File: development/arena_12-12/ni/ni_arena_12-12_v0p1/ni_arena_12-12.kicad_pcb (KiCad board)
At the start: 4 copper layers, 254 x 254 mm, 51 parts, among them J1 Barrel_Jack, J2 Conn_01x04, J3 Conn_01x04, P1 CONN15, P10 CONN15, P11 CONN15, P12 CONN15, P2 CONN15, P3 CONN15, P4 CONN15, P5 CONN15, P6 CONN15, P7 CONN15, P8 CONN15, P9 CONN15, Q2 MOSFET_NCHAN, SW1 SW_SPDT, U1 TXB0108PW, U18 Teensy4.1, U2 TXB0108PW, U3 TXB0108PW, U4 TXB0108PW, U5 TXB0108PW

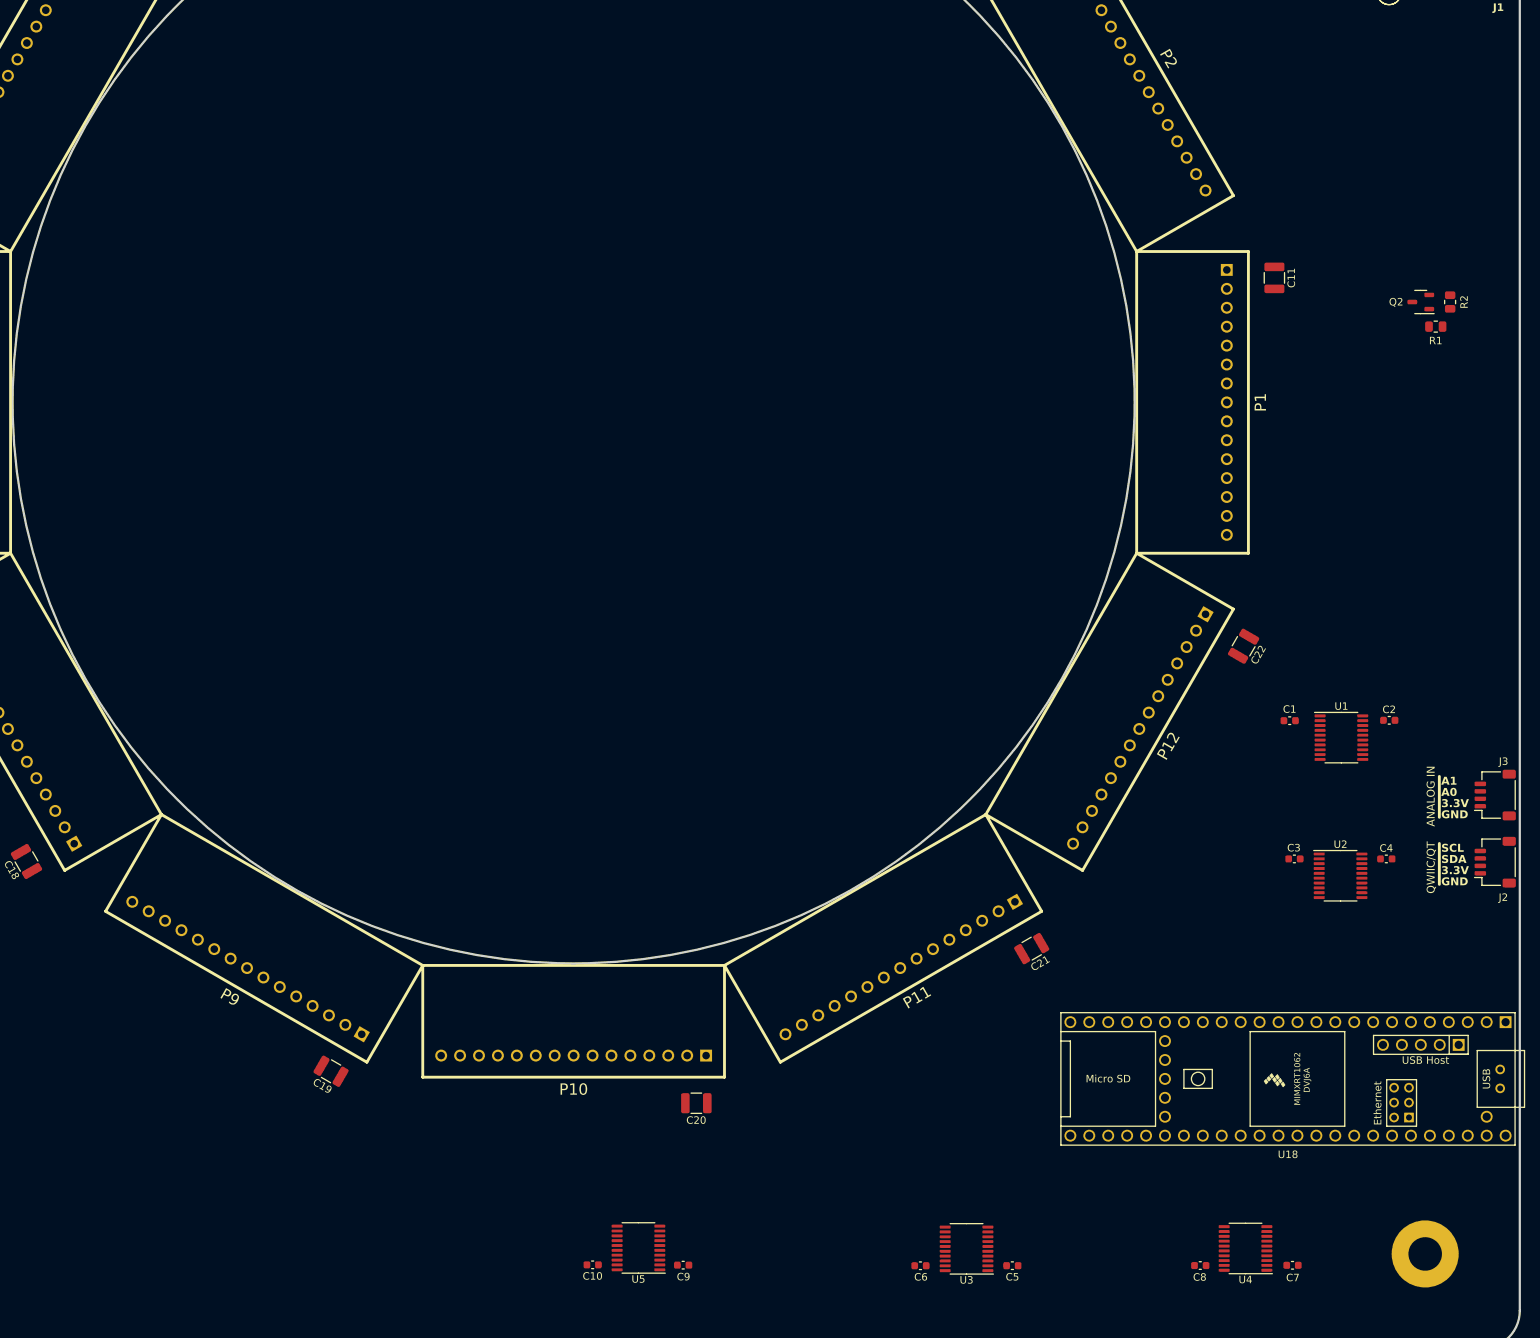
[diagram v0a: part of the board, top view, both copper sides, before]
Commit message: Finished initial schematic and layout for 12-12 NI arena (without voltage regulators).
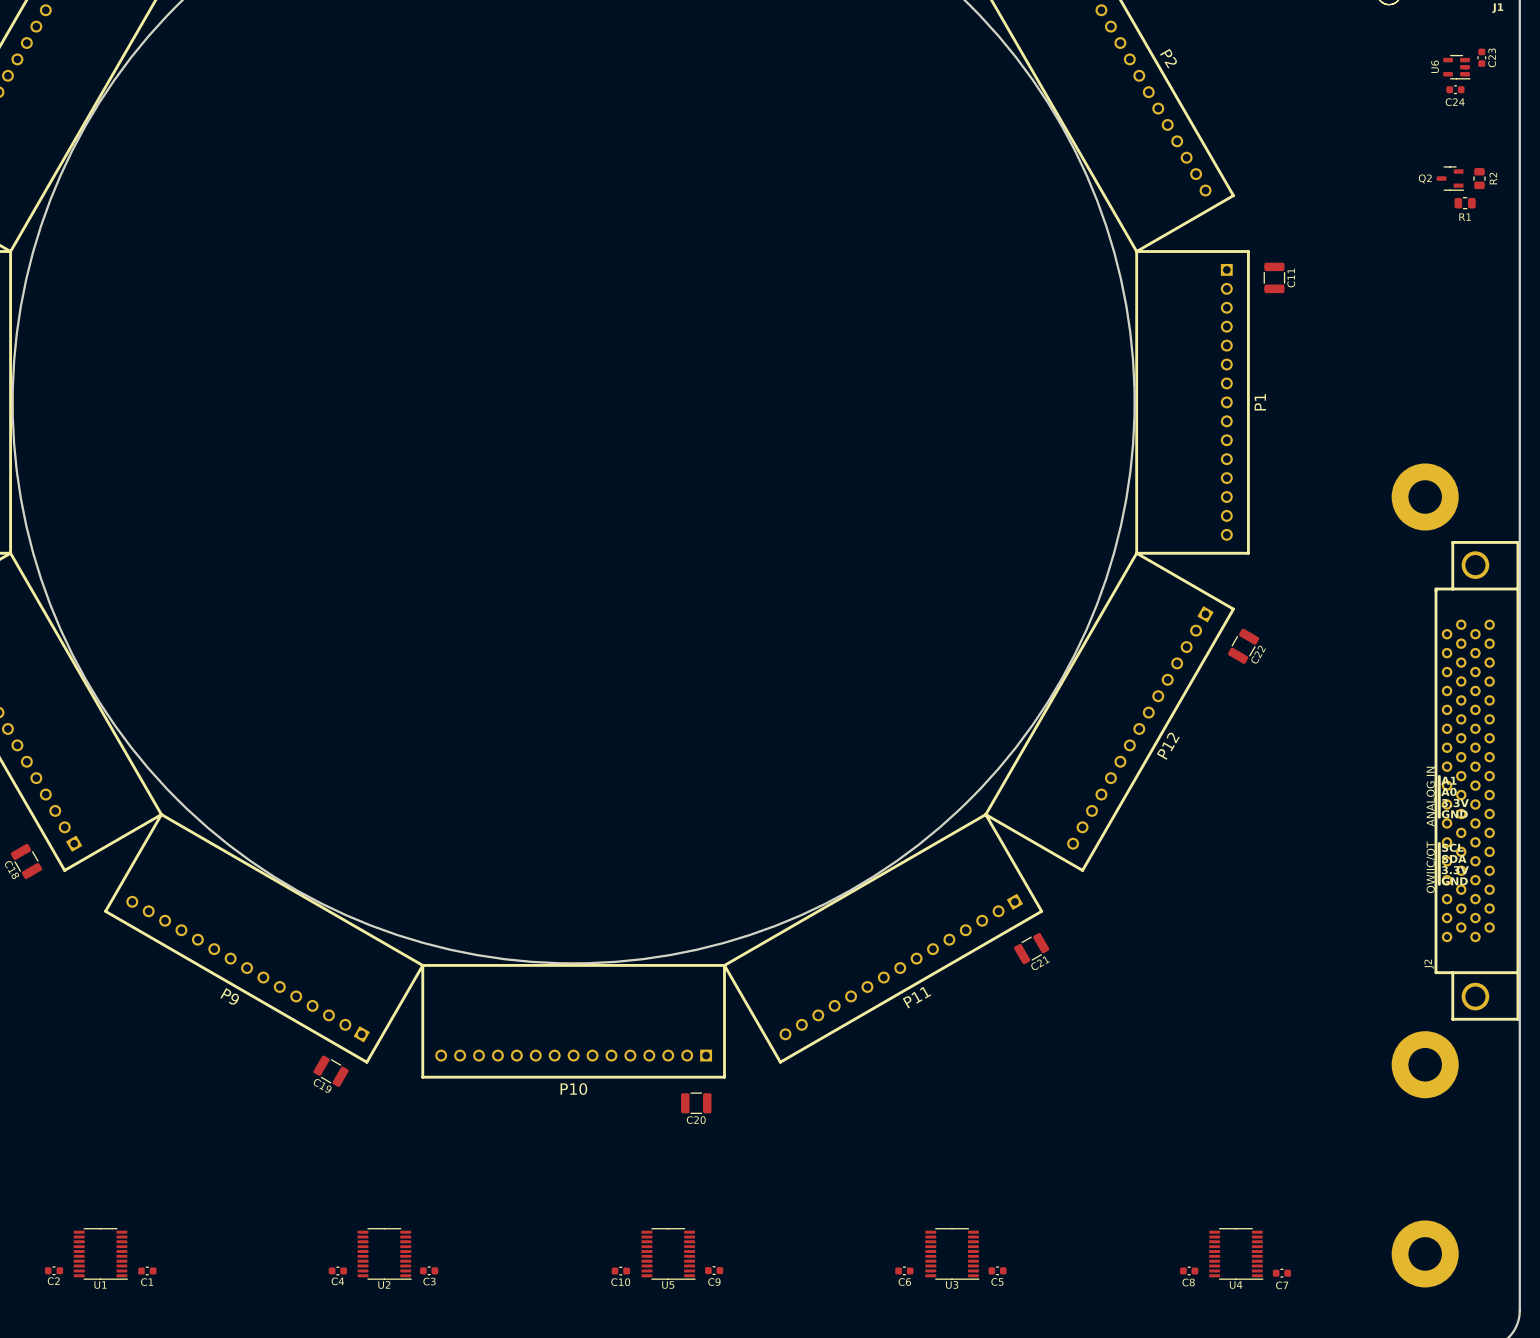
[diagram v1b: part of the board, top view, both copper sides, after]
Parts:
- removed J3: Conn_01x04, arena_custom:JST_SH_SM04B-SRSS-TB_1x04-1MP_P1.00mm_Horizontal
- removed U18: Teensy4.1, teensy:Teensy41
- added C23: 10uF, Capacitor_SMD:C_0603_1608Metric, F.Cu at (299.7, 131.5)
- added C24: 10uF, Capacitor_SMD:C_0603_1608Metric, F.Cu at (296.2, 135.8)
- added H5: MountingHole_Pad, MountingHole:MountingHole_4.5mm_Pad, F.Cu at (292.1, 190.5)
- added H6: MountingHole_Pad, MountingHole:MountingHole_4.5mm_Pad, F.Cu at (292.1, 266.7)
- added U6: AP2112K-3.3, Package_TO_SOT_SMD:SOT-23-5, F.Cu at (296.3, 132.8)
- J2: value Conn_01x04 -> NI_TE_68pos; footprint arena_custom:JST_SH_SM04B-SRSS-TB_1x04-1MP_P1.00mm_Horizontal -> arena_custom:TE_CONN_DSUB_RA_68
- moved C2 193.9 mm to (108.1, 294.4), turned to 180 degrees
- moved U1 180.4 mm to (114.3, 292.1), turned to 180 degrees
- moved C1 170.2 mm to (120.6, 294.4), turned to 0 degrees
- moved C4 151.2 mm to (146.2, 294.4), turned to 180 degrees
- moved U2 138.0 mm to (152.4, 292.1), turned to 180 degrees
- moved C3 128.6 mm to (158.4, 294.4), turned to 0 degrees
- moved Q2 17.0 mm to (295.4, 147.8)
- moved R1 17.0 mm to (297.5, 151.1)
- moved R2 17.0 mm to (299.4, 147.8)
- moved J2 11.3 mm to (304.6, 228.6)
- moved C9 4.21 mm to (196.7, 294.3)
- moved U5 4.08 mm to (190.5, 292.1)
- moved C10 3.87 mm to (184.1, 294.4)
- moved C6 2.27 mm to (222.2, 294.4)
- moved C5 2.11 mm to (234.7, 294.4)
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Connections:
- J2 pad 2: +3.3V -> GND
- J2 pad 3: /Teensy/SDA -> GND
- J2 pad 4: /Teensy/SCL -> unconnected-(J2-Pin_4-Pad4)
- P1 pad 12: unconnected-(P1-Pad12) -> /Level Shifters/PAN5V.CS_05
- P1 pad 13: unconnected-(P1-Pad13) -> /Level Shifters/PAN5V.CS_06
- P1 pad 14: unconnected-(P1-Pad14) -> /Level Shifters/PAN5V.CS_07
- P1 pad 4: /Level Shifters/PAN5V.SCK_0 -> /Level Shifters/PAN5V.SCK_00
- P1 pad 5: /Level Shifters/PAN5V.MOSI_0 -> /Level Shifters/PAN5V.MOSI_00
- P1 pad 6: /Level Shifters/PAN5V.MISO_0 -> /Level Shifters/PAN5V.MISO_00
- P10 pad 10: /Level Shifters/PAN5V.CS_18 -> /Level Shifters/PAN5V.CS_03
- P10 pad 11: /Level Shifters/PAN5V.CS_19 -> /Level Shifters/PAN5V.CS_04
- P10 pad 12: unconnected-(P10-Pad12) -> /Level Shifters/PAN5V.CS_05
- P10 pad 13: unconnected-(P10-Pad13) -> /Level Shifters/PAN5V.CS_06
- P10 pad 14: unconnected-(P10-Pad14) -> /Level Shifters/PAN5V.CS_07
- P10 pad 4: /Level Shifters/PAN5V.SCK_1 -> /Level Shifters/PAN5V.SCK_03
- P10 pad 5: /Level Shifters/PAN5V.MOSI_1 -> /Level Shifters/PAN5V.MOSI_09
- P10 pad 6: /Level Shifters/PAN5V.MISO_1 -> /Level Shifters/PAN5V.MISO_09
- P10 pad 7: /Level Shifters/PAN5V.CS_15 -> /Level Shifters/PAN5V.CS_00
- P10 pad 8: /Level Shifters/PAN5V.CS_16 -> /Level Shifters/PAN5V.CS_01
- P10 pad 9: /Level Shifters/PAN5V.CS_17 -> /Level Shifters/PAN5V.CS_02
- P11 pad 10: /Level Shifters/PAN5V.CS_23 -> /Level Shifters/PAN5V.CS_03
- P11 pad 11: /Level Shifters/PAN5V.CS_24 -> /Level Shifters/PAN5V.CS_04
- P11 pad 12: unconnected-(P11-Pad12) -> /Level Shifters/PAN5V.CS_05
- P11 pad 13: unconnected-(P11-Pad13) -> /Level Shifters/PAN5V.CS_06
- P11 pad 14: unconnected-(P11-Pad14) -> /Level Shifters/PAN5V.CS_07
- P11 pad 4: /Level Shifters/PAN5V.SCK_1 -> /Level Shifters/PAN5V.SCK_04
- P11 pad 5: /Level Shifters/PAN5V.MOSI_1 -> /Level Shifters/PAN5V.MOSI_10
- P11 pad 6: /Level Shifters/PAN5V.MISO_1 -> /Level Shifters/PAN5V.MISO_10
- P11 pad 7: /Level Shifters/PAN5V.CS_20 -> /Level Shifters/PAN5V.CS_00
- P11 pad 8: /Level Shifters/PAN5V.CS_21 -> /Level Shifters/PAN5V.CS_01
- P11 pad 9: /Level Shifters/PAN5V.CS_22 -> /Level Shifters/PAN5V.CS_02
- P12 pad 10: /Level Shifters/PAN5V.CS_28 -> /Level Shifters/PAN5V.CS_03
- P12 pad 11: /Level Shifters/PAN5V.CS_29 -> /Level Shifters/PAN5V.CS_04
- P12 pad 12: unconnected-(P12-Pad12) -> /Level Shifters/PAN5V.CS_05
- P12 pad 13: unconnected-(P12-Pad13) -> /Level Shifters/PAN5V.CS_06
- P12 pad 14: unconnected-(P12-Pad14) -> /Level Shifters/PAN5V.CS_07
- P12 pad 4: /Level Shifters/PAN5V.SCK_1 -> /Level Shifters/PAN5V.SCK_05
- P12 pad 5: /Level Shifters/PAN5V.MOSI_1 -> /Level Shifters/PAN5V.MOSI_11
- P12 pad 6: /Level Shifters/PAN5V.MISO_1 -> /Level Shifters/PAN5V.MISO_11
- P12 pad 7: /Level Shifters/PAN5V.CS_25 -> /Level Shifters/PAN5V.CS_00
- P12 pad 8: /Level Shifters/PAN5V.CS_26 -> /Level Shifters/PAN5V.CS_01
- P12 pad 9: /Level Shifters/PAN5V.CS_27 -> /Level Shifters/PAN5V.CS_02
- P2 pad 10: /Level Shifters/PAN5V.CS_08 -> /Level Shifters/PAN5V.CS_03
- P2 pad 11: /Level Shifters/PAN5V.CS_09 -> /Level Shifters/PAN5V.CS_04
- P2 pad 12: unconnected-(P2-Pad12) -> /Level Shifters/PAN5V.CS_05
- P2 pad 13: unconnected-(P2-Pad13) -> /Level Shifters/PAN5V.CS_06
- P2 pad 14: unconnected-(P2-Pad14) -> /Level Shifters/PAN5V.CS_07
- P2 pad 4: /Level Shifters/PAN5V.SCK_0 -> /Level Shifters/PAN5V.SCK_01
- P2 pad 5: /Level Shifters/PAN5V.MOSI_0 -> /Level Shifters/PAN5V.MOSI_01
- P2 pad 6: /Level Shifters/PAN5V.MISO_0 -> /Level Shifters/PAN5V.MISO_01
- P2 pad 7: /Level Shifters/PAN5V.CS_05 -> /Level Shifters/PAN5V.CS_00
- P2 pad 8: /Level Shifters/PAN5V.CS_06 -> /Level Shifters/PAN5V.CS_01
- P2 pad 9: /Level Shifters/PAN5V.CS_07 -> /Level Shifters/PAN5V.CS_02
- P3 pad 10: /Level Shifters/PAN5V.CS_13 -> /Level Shifters/PAN5V.CS_03
- P3 pad 11: /Level Shifters/PAN5V.CS_14 -> /Level Shifters/PAN5V.CS_04
- P3 pad 12: unconnected-(P3-Pad12) -> /Level Shifters/PAN5V.CS_05
- P3 pad 13: unconnected-(P3-Pad13) -> /Level Shifters/PAN5V.CS_06
- P3 pad 14: unconnected-(P3-Pad14) -> /Level Shifters/PAN5V.CS_07
- P3 pad 4: /Level Shifters/PAN5V.SCK_0 -> /Level Shifters/PAN5V.SCK_02
- P3 pad 5: /Level Shifters/PAN5V.MOSI_0 -> /Level Shifters/PAN5V.MOSI_02
- P3 pad 6: /Level Shifters/PAN5V.MISO_0 -> /Level Shifters/PAN5V.MISO_02
- P3 pad 7: /Level Shifters/PAN5V.CS_10 -> /Level Shifters/PAN5V.CS_00
- P3 pad 8: /Level Shifters/PAN5V.CS_11 -> /Level Shifters/PAN5V.CS_01
- P3 pad 9: /Level Shifters/PAN5V.CS_12 -> /Level Shifters/PAN5V.CS_02
- P4 pad 10: /Level Shifters/PAN5V.CS_18 -> /Level Shifters/PAN5V.CS_03
- P4 pad 11: /Level Shifters/PAN5V.CS_19 -> /Level Shifters/PAN5V.CS_04
- P4 pad 12: unconnected-(P4-Pad12) -> /Level Shifters/PAN5V.CS_05
- P4 pad 13: unconnected-(P4-Pad13) -> /Level Shifters/PAN5V.CS_06
- P4 pad 14: unconnected-(P4-Pad14) -> /Level Shifters/PAN5V.CS_07
- P4 pad 4: /Level Shifters/PAN5V.SCK_0 -> /Level Shifters/PAN5V.SCK_03
- P4 pad 5: /Level Shifters/PAN5V.MOSI_0 -> /Level Shifters/PAN5V.MOSI_03
- P4 pad 6: /Level Shifters/PAN5V.MISO_0 -> /Level Shifters/PAN5V.MISO_03
- P4 pad 7: /Level Shifters/PAN5V.CS_15 -> /Level Shifters/PAN5V.CS_00
- P4 pad 8: /Level Shifters/PAN5V.CS_16 -> /Level Shifters/PAN5V.CS_01
- P4 pad 9: /Level Shifters/PAN5V.CS_17 -> /Level Shifters/PAN5V.CS_02
- P5 pad 10: /Level Shifters/PAN5V.CS_23 -> /Level Shifters/PAN5V.CS_03
- P5 pad 11: /Level Shifters/PAN5V.CS_24 -> /Level Shifters/PAN5V.CS_04
- P5 pad 12: unconnected-(P5-Pad12) -> /Level Shifters/PAN5V.CS_05
- P5 pad 13: unconnected-(P5-Pad13) -> /Level Shifters/PAN5V.CS_06
- P5 pad 14: unconnected-(P5-Pad14) -> /Level Shifters/PAN5V.CS_07
- P5 pad 4: /Level Shifters/PAN5V.SCK_0 -> /Level Shifters/PAN5V.SCK_04
- P5 pad 5: /Level Shifters/PAN5V.MOSI_0 -> /Level Shifters/PAN5V.MOSI_04
- P5 pad 6: /Level Shifters/PAN5V.MISO_0 -> /Level Shifters/PAN5V.MISO_04
- P5 pad 7: /Level Shifters/PAN5V.CS_20 -> /Level Shifters/PAN5V.CS_00
- P5 pad 8: /Level Shifters/PAN5V.CS_21 -> /Level Shifters/PAN5V.CS_01
- P5 pad 9: /Level Shifters/PAN5V.CS_22 -> /Level Shifters/PAN5V.CS_02
- P6 pad 10: /Level Shifters/PAN5V.CS_28 -> /Level Shifters/PAN5V.CS_03
- P6 pad 11: /Level Shifters/PAN5V.CS_29 -> /Level Shifters/PAN5V.CS_04
- P6 pad 12: unconnected-(P6-Pad12) -> /Level Shifters/PAN5V.CS_05
- P6 pad 13: unconnected-(P6-Pad13) -> /Level Shifters/PAN5V.CS_06
- P6 pad 14: unconnected-(P6-Pad14) -> /Level Shifters/PAN5V.CS_07
- P6 pad 4: /Level Shifters/PAN5V.SCK_0 -> /Level Shifters/PAN5V.SCK_05
- P6 pad 5: /Level Shifters/PAN5V.MOSI_0 -> /Level Shifters/PAN5V.MOSI_05
- P6 pad 6: /Level Shifters/PAN5V.MISO_0 -> /Level Shifters/PAN5V.MISO_05
- P6 pad 7: /Level Shifters/PAN5V.CS_25 -> /Level Shifters/PAN5V.CS_00
- P6 pad 8: /Level Shifters/PAN5V.CS_26 -> /Level Shifters/PAN5V.CS_01
- P6 pad 9: /Level Shifters/PAN5V.CS_27 -> /Level Shifters/PAN5V.CS_02
- P7 pad 12: unconnected-(P7-Pad12) -> /Level Shifters/PAN5V.CS_05
- P7 pad 13: unconnected-(P7-Pad13) -> /Level Shifters/PAN5V.CS_06
- P7 pad 14: unconnected-(P7-Pad14) -> /Level Shifters/PAN5V.CS_07
- P7 pad 4: /Level Shifters/PAN5V.SCK_1 -> /Level Shifters/PAN5V.SCK_00
- P7 pad 5: /Level Shifters/PAN5V.MOSI_1 -> /Level Shifters/PAN5V.MOSI_06
- P7 pad 6: /Level Shifters/PAN5V.MISO_1 -> /Level Shifters/PAN5V.MISO_06
- P8 pad 10: /Level Shifters/PAN5V.CS_08 -> /Level Shifters/PAN5V.CS_03
- P8 pad 11: /Level Shifters/PAN5V.CS_09 -> /Level Shifters/PAN5V.CS_04
- P8 pad 12: unconnected-(P8-Pad12) -> /Level Shifters/PAN5V.CS_05
- P8 pad 13: unconnected-(P8-Pad13) -> /Level Shifters/PAN5V.CS_06
- P8 pad 14: unconnected-(P8-Pad14) -> /Level Shifters/PAN5V.CS_07
- P8 pad 4: /Level Shifters/PAN5V.SCK_1 -> /Level Shifters/PAN5V.SCK_01
- P8 pad 5: /Level Shifters/PAN5V.MOSI_1 -> /Level Shifters/PAN5V.MOSI_07
- P8 pad 6: /Level Shifters/PAN5V.MISO_1 -> /Level Shifters/PAN5V.MISO_07
- P8 pad 7: /Level Shifters/PAN5V.CS_05 -> /Level Shifters/PAN5V.CS_00
- P8 pad 8: /Level Shifters/PAN5V.CS_06 -> /Level Shifters/PAN5V.CS_01
- P8 pad 9: /Level Shifters/PAN5V.CS_07 -> /Level Shifters/PAN5V.CS_02
- P9 pad 10: /Level Shifters/PAN5V.CS_13 -> /Level Shifters/PAN5V.CS_03
- P9 pad 11: /Level Shifters/PAN5V.CS_14 -> /Level Shifters/PAN5V.CS_04
- P9 pad 12: unconnected-(P9-Pad12) -> /Level Shifters/PAN5V.CS_05
- P9 pad 13: unconnected-(P9-Pad13) -> /Level Shifters/PAN5V.CS_06
- P9 pad 14: unconnected-(P9-Pad14) -> /Level Shifters/PAN5V.CS_07
- P9 pad 4: /Level Shifters/PAN5V.SCK_1 -> /Level Shifters/PAN5V.SCK_02
- P9 pad 5: /Level Shifters/PAN5V.MOSI_1 -> /Level Shifters/PAN5V.MOSI_08
- P9 pad 6: /Level Shifters/PAN5V.MISO_1 -> /Level Shifters/PAN5V.MISO_08
- P9 pad 7: /Level Shifters/PAN5V.CS_10 -> /Level Shifters/PAN5V.CS_00
- P9 pad 8: /Level Shifters/PAN5V.CS_11 -> /Level Shifters/PAN5V.CS_01
- P9 pad 9: /Level Shifters/PAN5V.CS_12 -> /Level Shifters/PAN5V.CS_02
- U1 pad 1: /Level Shifters/PAN3V.RESET -> /Level Shifters/PAN3V.CS_00
- U1 pad 12: /Level Shifters/PAN5V.MISO_1 -> /Level Shifters/PAN5V.CS_07
- U1 pad 13: /Level Shifters/PAN5V.MOSI_1 -> /Level Shifters/PAN5V.CS_06
- U1 pad 14: /Level Shifters/PAN5V.SCK_1 -> /Level Shifters/PAN5V.CS_05
- U1 pad 15: unconnected-(U1-B5-Pad15) -> /Level Shifters/PAN5V.CS_04
- U1 pad 16: /Level Shifters/PAN5V.MISO_0 -> /Level Shifters/PAN5V.CS_03
- U1 pad 17: /Level Shifters/PAN5V.MOSI_0 -> /Level Shifters/PAN5V.CS_02
- U1 pad 18: /Level Shifters/PAN5V.SCK_0 -> /Level Shifters/PAN5V.CS_01
- U1 pad 20: /Level Shifters/PAN5V.RESET -> /Level Shifters/PAN5V.CS_00
- U1 pad 3: /Level Shifters/PAN3V.SCK_0 -> /Level Shifters/PAN3V.CS_01
- U1 pad 4: /Level Shifters/PAN3V.MOSI_0 -> /Level Shifters/PAN3V.CS_02
- U1 pad 5: /Level Shifters/PAN3V.MISO_0 -> /Level Shifters/PAN3V.CS_03
- U1 pad 6: unconnected-(U1-A5-Pad6) -> /Level Shifters/PAN3V.CS_04
- U1 pad 7: /Level Shifters/PAN3V.SCK_1 -> /Level Shifters/PAN3V.CS_05
- U1 pad 8: /Level Shifters/PAN3V.MOSI_1 -> /Level Shifters/PAN3V.CS_06
- U1 pad 9: /Level Shifters/PAN3V.MISO_1 -> /Level Shifters/PAN3V.CS_07
- U2 pad 1: /Level Shifters/PAN3V.CS_00 -> /Level Shifters/PAN3V.SCK_00
- U2 pad 12: /Level Shifters/PAN5V.CS_07 -> /Level Shifters/PAN5V.MISO_00
- U2 pad 13: /Level Shifters/PAN5V.CS_06 -> /Level Shifters/PAN5V.MOSI_00
- U2 pad 14: /Level Shifters/PAN5V.CS_05 -> /Level Shifters/PAN5V.SCK_05
- U2 pad 15: /Level Shifters/PAN5V.CS_04 -> /Level Shifters/PAN5V.SCK_04
- U2 pad 16: /Level Shifters/PAN5V.CS_03 -> /Level Shifters/PAN5V.SCK_03
- U2 pad 17: /Level Shifters/PAN5V.CS_02 -> /Level Shifters/PAN5V.SCK_02
- U2 pad 18: /Level Shifters/PAN5V.CS_01 -> /Level Shifters/PAN5V.SCK_01
- U2 pad 20: /Level Shifters/PAN5V.CS_00 -> /Level Shifters/PAN5V.SCK_00
- U2 pad 3: /Level Shifters/PAN3V.CS_01 -> /Level Shifters/PAN3V.SCK_01
- U2 pad 4: /Level Shifters/PAN3V.CS_02 -> /Level Shifters/PAN3V.SCK_02
- U2 pad 5: /Level Shifters/PAN3V.CS_03 -> /Level Shifters/PAN3V.SCK_03
- U2 pad 6: /Level Shifters/PAN3V.CS_04 -> /Level Shifters/PAN3V.SCK_04
- U2 pad 7: /Level Shifters/PAN3V.CS_05 -> /Level Shifters/PAN3V.SCK_05
- U2 pad 8: /Level Shifters/PAN3V.CS_06 -> /Level Shifters/PAN3V.MOSI_00
- U2 pad 9: /Level Shifters/PAN3V.CS_07 -> /Level Shifters/PAN3V.MISO_00
- U3 pad 1: /Level Shifters/PAN3V.CS_08 -> /Level Shifters/PAN3V.MOSI_01
- U3 pad 12: /Level Shifters/PAN5V.CS_15 -> /Level Shifters/PAN5V.MISO_04
- U3 pad 13: /Level Shifters/PAN5V.CS_14 -> /Level Shifters/PAN5V.MOSI_04
- U3 pad 14: /Level Shifters/PAN5V.CS_13 -> /Level Shifters/PAN5V.MISO_03
- U3 pad 15: /Level Shifters/PAN5V.CS_12 -> /Level Shifters/PAN5V.MOSI_03
- U3 pad 16: /Level Shifters/PAN5V.CS_11 -> /Level Shifters/PAN5V.MISO_02
- U3 pad 17: /Level Shifters/PAN5V.CS_10 -> /Level Shifters/PAN5V.MOSI_02
- U3 pad 18: /Level Shifters/PAN5V.CS_09 -> /Level Shifters/PAN5V.MISO_01
- U3 pad 20: /Level Shifters/PAN5V.CS_08 -> /Level Shifters/PAN5V.MOSI_01
- U3 pad 3: /Level Shifters/PAN3V.CS_09 -> /Level Shifters/PAN3V.MISO_01
- U3 pad 4: /Level Shifters/PAN3V.CS_10 -> /Level Shifters/PAN3V.MOSI_02
- U3 pad 5: /Level Shifters/PAN3V.CS_11 -> /Level Shifters/PAN3V.MISO_02
- U3 pad 6: /Level Shifters/PAN3V.CS_12 -> /Level Shifters/PAN3V.MOSI_03
- U3 pad 7: /Level Shifters/PAN3V.CS_13 -> /Level Shifters/PAN3V.MISO_03
- U3 pad 8: /Level Shifters/PAN3V.CS_14 -> /Level Shifters/PAN3V.MOSI_04
- U3 pad 9: /Level Shifters/PAN3V.CS_15 -> /Level Shifters/PAN3V.MISO_04
- U4 pad 1: /Level Shifters/PAN3V.CS_16 -> /Level Shifters/PAN3V.MOSI_05
- U4 pad 12: /Level Shifters/PAN5V.CS_23 -> /Level Shifters/PAN5V.MISO_08
- U4 pad 13: /Level Shifters/PAN5V.CS_22 -> /Level Shifters/PAN5V.MOSI_08
- U4 pad 14: /Level Shifters/PAN5V.CS_21 -> /Level Shifters/PAN5V.MISO_07
- U4 pad 15: /Level Shifters/PAN5V.CS_20 -> /Level Shifters/PAN5V.MOSI_07
- U4 pad 16: /Level Shifters/PAN5V.CS_19 -> /Level Shifters/PAN5V.MISO_06
- U4 pad 17: /Level Shifters/PAN5V.CS_18 -> /Level Shifters/PAN5V.MOSI_06
- U4 pad 18: /Level Shifters/PAN5V.CS_17 -> /Level Shifters/PAN5V.MISO_05
- U4 pad 20: /Level Shifters/PAN5V.CS_16 -> /Level Shifters/PAN5V.MOSI_05
- U4 pad 3: /Level Shifters/PAN3V.CS_17 -> /Level Shifters/PAN3V.MISO_05
- U4 pad 4: /Level Shifters/PAN3V.CS_18 -> /Level Shifters/PAN3V.MOSI_06
- U4 pad 5: /Level Shifters/PAN3V.CS_19 -> /Level Shifters/PAN3V.MISO_06
- U4 pad 6: /Level Shifters/PAN3V.CS_20 -> /Level Shifters/PAN3V.MOSI_07
- U4 pad 7: /Level Shifters/PAN3V.CS_21 -> /Level Shifters/PAN3V.MISO_07
- U4 pad 8: /Level Shifters/PAN3V.CS_22 -> /Level Shifters/PAN3V.MOSI_08
- U4 pad 9: /Level Shifters/PAN3V.CS_23 -> /Level Shifters/PAN3V.MISO_08
- U5 pad 1: /Level Shifters/PAN3V.CS_24 -> /Level Shifters/PAN3V.MOSI_09
- U5 pad 12: /Level Shifters/PAN5V.EXT_INT -> /Level Shifters/PAN5V.RESET
- U5 pad 13: unconnected-(U5-B7-Pad13) -> /Level Shifters/PAN5V.EXT_INT
- U5 pad 14: /Level Shifters/PAN5V.CS_29 -> /Level Shifters/PAN5V.MISO_11
- U5 pad 15: /Level Shifters/PAN5V.CS_28 -> /Level Shifters/PAN5V.MOSI_11
- U5 pad 16: /Level Shifters/PAN5V.CS_27 -> /Level Shifters/PAN5V.MISO_10
- U5 pad 17: /Level Shifters/PAN5V.CS_26 -> /Level Shifters/PAN5V.MOSI_10
- U5 pad 18: /Level Shifters/PAN5V.CS_25 -> /Level Shifters/PAN5V.MISO_09
- U5 pad 20: /Level Shifters/PAN5V.CS_24 -> /Level Shifters/PAN5V.MOSI_09
- U5 pad 3: /Level Shifters/PAN3V.CS_25 -> /Level Shifters/PAN3V.MISO_09
- U5 pad 4: /Level Shifters/PAN3V.CS_26 -> /Level Shifters/PAN3V.MOSI_10
- U5 pad 5: /Level Shifters/PAN3V.CS_27 -> /Level Shifters/PAN3V.MISO_10
- U5 pad 6: /Level Shifters/PAN3V.CS_28 -> /Level Shifters/PAN3V.MOSI_11
- U5 pad 7: /Level Shifters/PAN3V.CS_29 -> /Level Shifters/PAN3V.MISO_11
- U5 pad 8: unconnected-(U5-A7-Pad8) -> /Level Shifters/PAN3V.EXT_INT
- U5 pad 9: /Level Shifters/PAN3V.EXT_INT -> /Level Shifters/PAN3V.RESET

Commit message: Worked on 12-12 arenas.
Resized 12-12 arenas,   changed NI connector from right angle to
vertical, push panals back by 1mm.
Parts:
- J2: footprint arena_custom:TE_CONN_DSUB_RA_68 -> arena_custom:TE_CONN_DSUB_VERT_68; moved to B.Cu
- moved SW1 28.7 mm to (287.0, 112.1)
- moved J1 27.5 mm to (292.0, 92.0)
- moved J2 22.7 mm to (285.8, 215.9)
- moved H3 18.0 mm to (279.4, 279.4)
- moved H2 18.0 mm to (279.4, 76.2)
- moved H4 18.0 mm to (76.2, 279.4)
- moved H1 18.0 mm to (76.2, 76.2)
- moved C2 15.3 mm to (94.3, 287.6)
- moved C3 15.3 mm to (144.6, 287.6)
- moved U2 15.3 mm to (138.6, 285.4)
- moved U3 15.3 mm to (214.8, 285.4)
- moved U5 15.3 mm to (176.7, 285.4)
- moved U1 15.3 mm to (100.5, 285.4)
- moved C1 15.3 mm to (106.8, 287.7)
- moved C10 15.3 mm to (170.3, 287.7)
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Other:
- board size 254 x 254 mm -> 228.6 x 228.6 mm
- board text added: "NI 12-12 Arena V0.1 R1"
- board text removed: "3.3V"
- board text removed: "A0"
- board text removed: "A1"
- board text removed: "ANALOG IN"
- board text removed: "GND"
- board text removed: "QWIIC/QT"
- board text removed: "SCL"
- board text removed: "SDA"
- board text removed: "Teensy 12-12 Controller-Arena V0.1 R1"

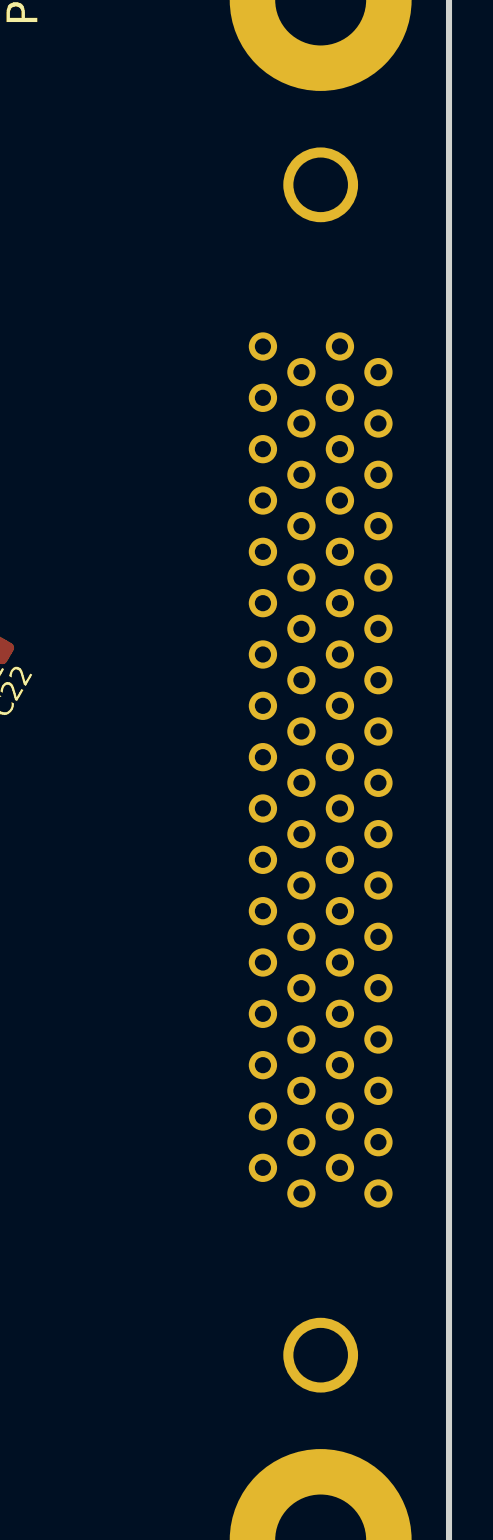
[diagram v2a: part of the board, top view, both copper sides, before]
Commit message: Added work on switching regulator.
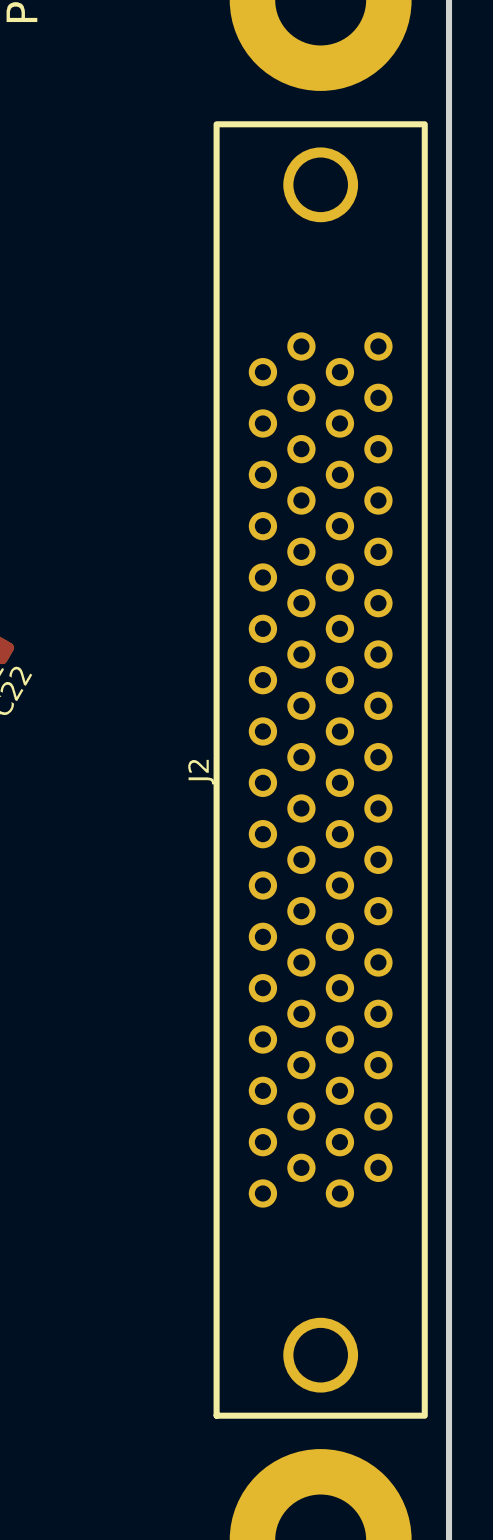
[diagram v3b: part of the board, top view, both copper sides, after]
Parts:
- J2: moved to F.Cu

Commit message: Worked on layout for 12-12 NI arena w/ vreg.
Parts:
- moved H5 12.7 mm to (285.8, 190.5)
- moved H6 12.7 mm to (285.8, 266.7)
- moved J2 12.7 mm to (285.8, 228.6)
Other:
- outline, holes or cut-outs redrawn
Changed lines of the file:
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@@
   )
   (footprint "MountingHole:MountingHole_4.5mm_Pad" (layer "F.Cu")
-    (at 285.75 177.8)
+    (at 285.75 190.5)
     (descr "Mounting Hole 4.5mm")
     (tags "mounting hole 4.5mm")
@@
   )
   (footprint "MountingHole:MountingHole_4.5mm_Pad" (layer "F.Cu")
-    (at 285.75 254)
+    (at 285.75 266.7)
     (descr "Mounting Hole 4.5mm")
     (tags "mounting hole 4.5mm")
@@
   )
   (footprint "arena_custom:TE_CONN_DSUB_VERT_68" (layer "F.Cu")
-    (at 285.75 215.9 90)
+    (at 285.75 228.6 90)
     (property "Sheetfile" "ni_connector.kicad_sch")
     (property "Sheetname" "NI Connector")
@@
   (gr_line (start 63.5 69.85) (end 63.5 285.75)
     (stroke (width 0.3) (type default)) (layer "Edge.Cuts"))
-  (gr_circle (center 177.8 177.8) (end 256.3 177.8)
+  (gr_circle (center 177.8 177.8) (end 254.508 177.8)
     (stroke (width 0.3) (type default)) (fill none) (layer "Edge.Cuts"))
   (gr_line (start 292.1 285.75) (end 292.1 69.85)
